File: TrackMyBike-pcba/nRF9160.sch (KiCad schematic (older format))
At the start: 1 part

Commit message: Add project description
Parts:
- U?: symbol NRF9160-SICA-R:NRF9160-SICA-R -> TrackMyBike-pcba-rescue:NRF9160-SICA-R-NRF9160-SICA-R
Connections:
- net GND: now reaches U?.1 (GND_SHIELD), U?.14 (GND_SHIELD), U?.17 (GND_SHIELD), U?.21 (GND_SHIELD), U?.27 (GND_SHIELD), U?.31 (GND_SHIELD), U?.36 (GND_SHIELD), U?.41 (GND_SHIELD), U?.44 (GND_SHIELD), U?.47 (GND_SHIELD), U?.5 (GND_SHIELD), U?.50 (GND_SHIELD), U?.52 (GND_SHIELD), U?.56 (GND_SHIELD), U?.60 (GND_SHIELD), U?.62 (GND_SHIELD), U?.63 (GND_SHIELD), U?.65 (GND_SHIELD), U?.66 (GND_SHIELD), U?.72 (GND_SHIELD), U?.74 (GND_SHIELD), U?.75 (GND_SHIELD), U?.76 (GND_SHIELD), U?.77 (GND_SHIELD), U?.78 (GND_SHIELD), U?.79 (GND_SHIELD), U?.80 (GND_SHIELD), U?.81 (GND_SHIELD), U?.82 (GND_SHIELD), U?.85 (GND_SHIELD), U?.9 (GND_SHIELD), U?.90 (GND_SHIELD), U?.94 (GND_SHIELD), U?.98 (GND_SHIELD)
- net GND: now also U?.103_1 (VSS), U?.103_10 (VSS), U?.103_11 (VSS), U?.103_12 (VSS), U?.103_13 (VSS), U?.103_14 (VSS), U?.103_15 (VSS), U?.103_16 (VSS), U?.103_17 (VSS), U?.103_18 (VSS), U?.103_19 (VSS), U?.103_2 (VSS), U?.103_20 (VSS), U?.103_21 (VSS), U?.103_22 (VSS), U?.103_23 (VSS), U?.103_24 (VSS), U?.103_25 (VSS), U?.103_26 (VSS), U?.103_27 (VSS), U?.103_28 (VSS), U?.103_29 (VSS), U?.103_3 (VSS), U?.103_30 (VSS), U?.103_31 (VSS), U?.103_32 (VSS), U?.103_33 (VSS), U?.103_34 (VSS), U?.103_35 (VSS), U?.103_4 (VSS), U?.103_5 (VSS), U?.103_6 (VSS), U?.103_7 (VSS), U?.103_8 (VSS), U?.103_9 (VSS)
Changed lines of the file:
@@
 $EndDescr
 $Comp
-L NRF9160-SICA-R:NRF9160-SICA-R U?
+L TrackMyBike-pcba-rescue:NRF9160-SICA-R-NRF9160-SICA-R U?
 U 1 1 5F168AEC
 P 5600 3650
+AR Path="/5F168AEC" Ref="U?"  Part="1"
+AR Path="/5F16898F/5F168AEC" Ref="U?"  Part="1"
 F 0 "U?" H 5600 5917 50  0000 C CNN
 F 1 "NRF9160-SICA-R" H 5600 5826 50  0000 C CNN
@@
 	1    0    0    -1
 $EndComp
+$Comp
+L power:GND #PWR?
+U 1 1 5F174F94
+P 6950 5650
+F 0 "#PWR?" H 6950 5400 50  0001 C CNN
+F 1 "GND" H 6955 5477 50  0000 C CNN
+F 2 "" H 6950 5650 50  0001 C CNN
+F 3 "" H 6950 5650 50  0001 C CNN
+	1    6950 5650
+	1    0    0    -1
+$EndComp
+Wire Wire Line
+	6600 5650 6950 5650
+Wire Wire Line
+	6950 5650 6950 5550
+Wire Wire Line
+	6950 5550 6600 5550
+Connection ~ 6950 5650
 $EndSCHEMATC

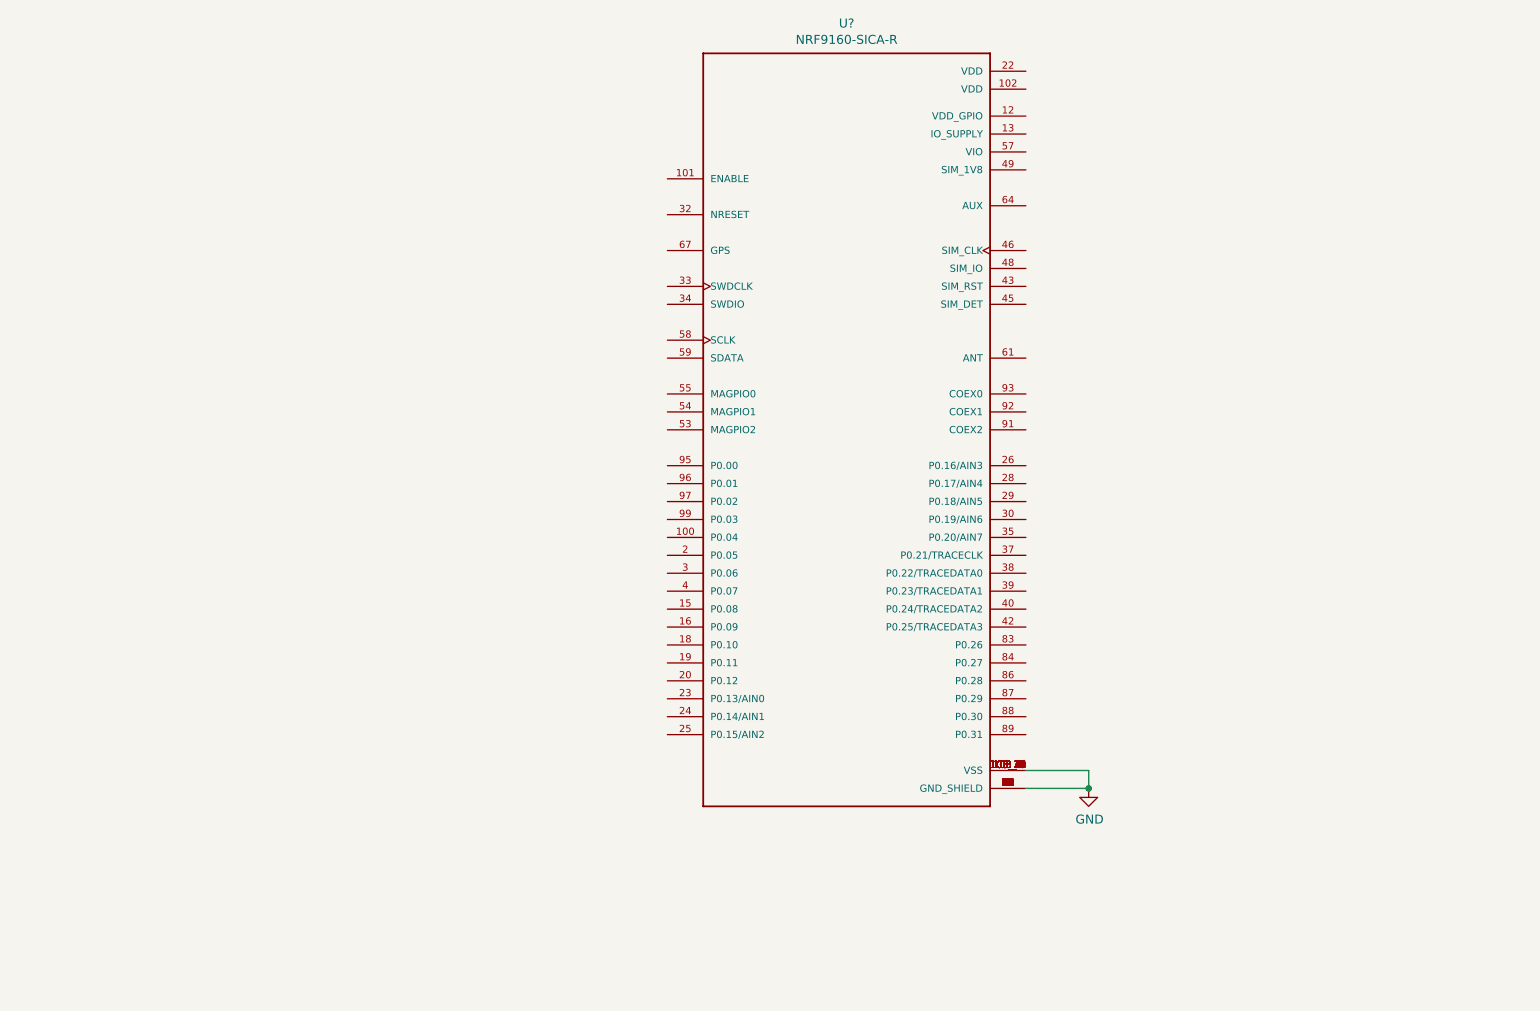
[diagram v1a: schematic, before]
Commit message: Add SIM card, FTDI IC
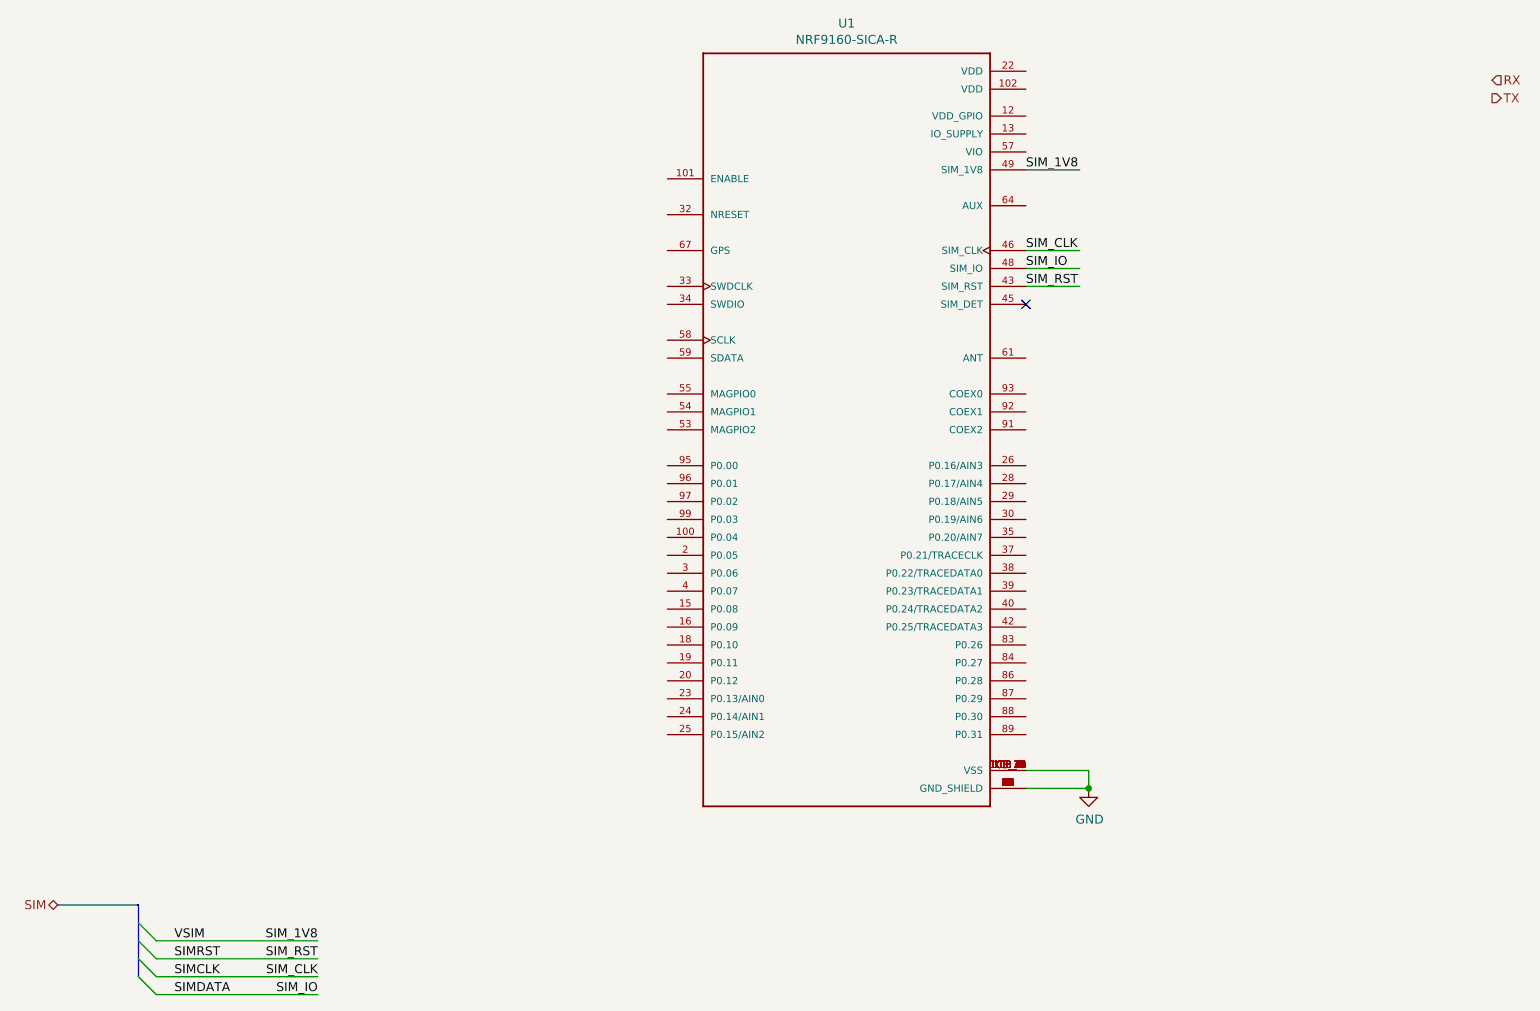
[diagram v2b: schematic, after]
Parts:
- gave numbers to parts that had none: 1
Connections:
- net labels added: RX, SIM, SIMCLK, SIMDATA, SIMRST, SIM_1V8, SIM_CLK, SIM_IO, SIM_RST, TX, VSIM
- wire segments 3 -> 11
- no-connect marks 0 -> 1
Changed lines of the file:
@@
 P 5600 3650
 AR Path="/5F168AEC" Ref="U?"  Part="1"
-AR Path="/5F16898F/5F168AEC" Ref="U?"  Part="1"
-F 0 "U?" H 5600 5917 50  0000 C CNN
+AR Path="/5F16898F/5F168AEC" Ref="U1"  Part="1"
+F 0 "U1" H 5600 5917 50  0000 C CNN
 F 1 "NRF9160-SICA-R" H 5600 5826 50  0000 C CNN
 F 2 "NORDIC_NRF9160-SICA-R" H 6000 5850 50  0001 L BNN
@@
 $EndComp
 $Comp
-L power:GND #PWR?
+L power:GND #PWR0107
 U 1 1 5F174F94
 P 6950 5650
-F 0 "#PWR?" H 6950 5400 50  0001 C CNN
+F 0 "#PWR0107" H 6950 5400 50  0001 C CNN
 F 1 "GND" H 6955 5477 50  0000 C CNN
 F 2 "" H 6950 5650 50  0001 C CNN
@@
 	6950 5550 6600 5550
 Connection ~ 6950 5650
+Text Label 1850 6500 0    50   ~ 0
+VSIM
+Text Label 1850 6600 0    50   ~ 0
+SIMRST
+Text Label 1850 6700 0    50   ~ 0
+SIMCLK
+Text Label 1850 6800 0    50   ~ 0
+SIMDATA
+Text HLabel 1200 6300 0    50   BiDi ~ 0
+SIM
+Wire Bus Line
+	1200 6300 1650 6300
+Entry Wire Line
+	1650 6400 1750 6500
+Entry Wire Line
+	1650 6500 1750 6600
+Entry Wire Line
+	1650 6600 1750 6700
+Entry Wire Line
+	1650 6700 1750 6800
+NoConn ~ 6600 2950
+Text Label 6600 2650 0    50   ~ 0
+SIM_CLK
+Text Label 6600 2750 0    50   ~ 0
+SIM_IO
+Text Label 6600 2850 0    50   ~ 0
+SIM_RST
+Wire Wire Line
+	6600 2650 6900 2650
+Wire Wire Line
+	6600 2750 6900 2750
+Wire Wire Line
+	6600 2850 6900 2850
+Wire Wire Line
+	6600 2200 6900 2200
+Text Label 6600 2200 0    50   ~ 0
+SIM_1V8
+Text Label 2650 6500 2    50   ~ 0
+SIM_1V8
+Text Label 2650 6600 2    50   ~ 0
+SIM_RST
+Text Label 2650 6700 2    50   ~ 0
+SIM_CLK
+Wire Wire Line
+	1750 6500 2650 6500
+Wire Wire Line
+	1750 6700 2650 6700
+Wire Wire Line
+	1750 6600 2650 6600
+Wire Wire Line
+	1750 6800 2650 6800
+Text Label 2650 6800 2    50   ~ 0
+SIM_IO
+Text HLabel 9200 1700 2    50   Input ~ 0
+RX
+Text HLabel 9200 1800 2    50   Output ~ 0
+TX
+Wire Bus Line
+	1650 6300 1650 6700
 $EndSCHEMATC

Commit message: Add TX/RX to nRF9160
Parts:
- U1: symbol TrackMyBike-pcba-rescue:NRF9160-SICA-R-NRF9160-SICA-R -> NRF9160-SICA-R:NRF9160-SICA-R
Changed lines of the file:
@@
 $EndDescr
 $Comp
-L TrackMyBike-pcba-rescue:NRF9160-SICA-R-NRF9160-SICA-R U?
+L NRF9160-SICA-R:NRF9160-SICA-R U?
 U 1 1 5F168AEC
 P 5600 3650
